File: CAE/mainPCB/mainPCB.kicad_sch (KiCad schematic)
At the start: 30 parts, among them J1 DHT22_CVT, J10 V_in_01, J12 LORA, J13 GPS_NEO, J14 VL6180X_01, J15 VL6180X_02, J2 V_In, J3 LM3144_CVT, J4 LM3144_RPM, J5 DS18B20_01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

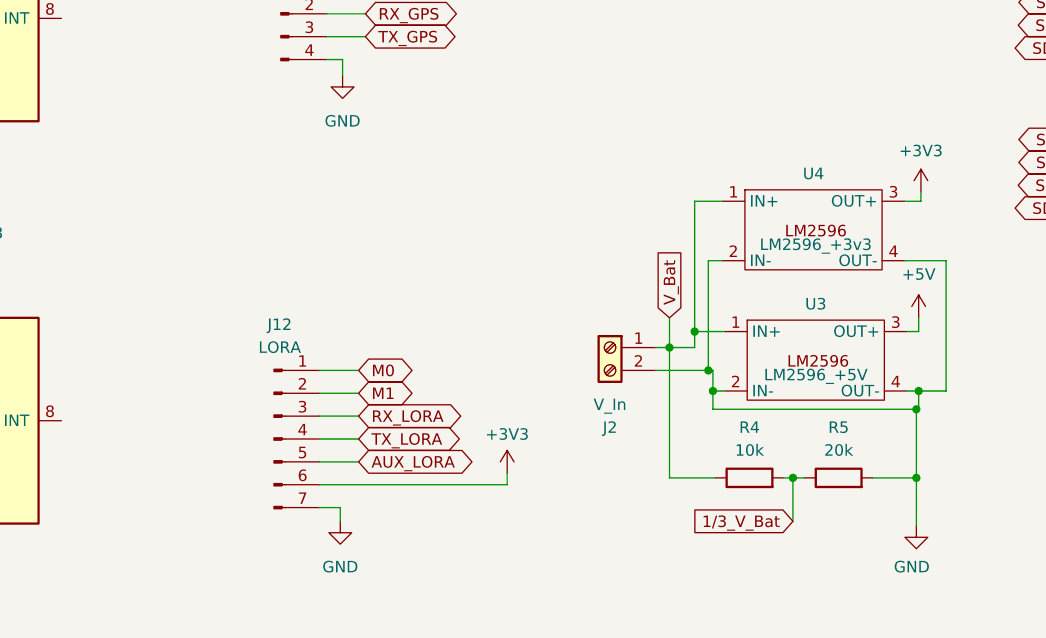
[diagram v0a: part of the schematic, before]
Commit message: PCB updated
3D models added, rewiring for milling
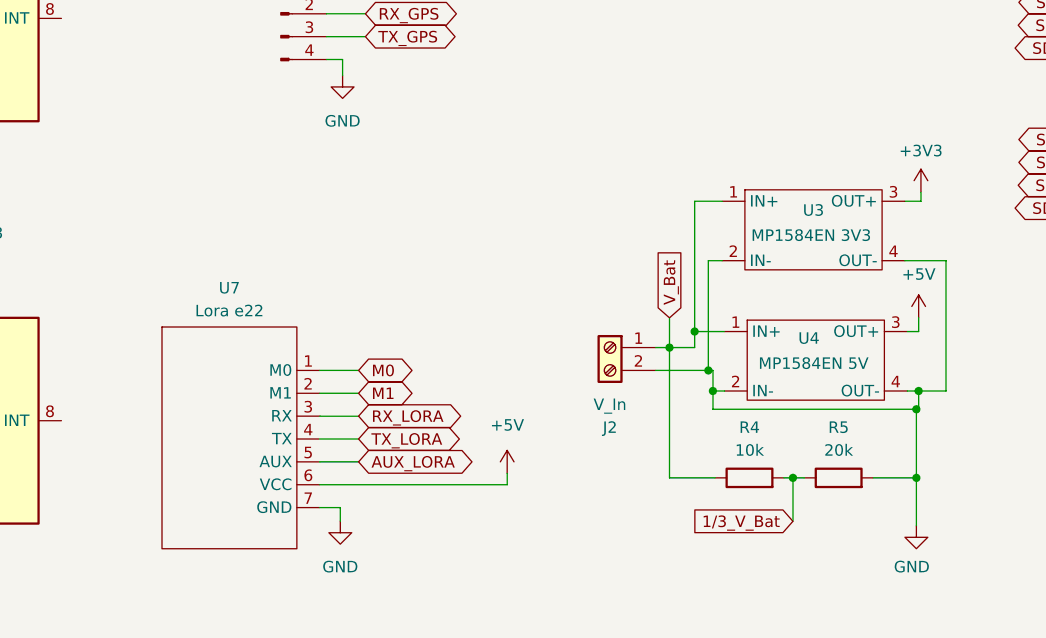
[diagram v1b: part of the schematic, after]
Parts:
- removed J12: LORA, Connector_PinHeader_2.54mm:PinHeader_1x07_P2.54mm_Vertical, symbol Connector:Conn_01x07_Pin
- removed U3: LM2596_+5V, DC_DC_LM2596_small:DC_DC_LM2596_small, symbol custom_symbols:LM2596
- removed U4: LM2596_+3v3, DC_DC_LM2596_small:DC_DC_LM2596_small, symbol custom_symbols:LM2596
- added U3: MP1584EN 3V3, custom:MP1584EN, symbol custom_symbols:MP1584EN
- added U4: MP1584EN 5V, custom:MP1584EN, symbol custom_symbols:MP1584EN
- added U7: Lora e22, custom:lora_e22, symbol custom_symbols:lora_e22
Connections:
- net +3V3: now also U3.3 (OUT+)
- net +5V: now also U4.3 (OUT+), U7.6 (VCC)
- net AUX_LORA: now also U7.5 (AUX)
- net GND: now also U3.2 (IN-), U3.4 (OUT-), U4.2 (IN-), U4.4 (OUT-), U7.7 (GND)
- net M0: now also U7.1 (M0)
- net M1: now also U7.2 (M1)
- net RX_LORA: now also U7.3 (RX)
- net TX_LORA: now also U7.4 (TX)
- net V_Bat: now also U3.1 (IN+), U4.1 (IN+)
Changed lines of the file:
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@@
-    )
-  )
-  (symbol (lib_id "custom_symbols:LM2596") (at 131.064 158.75 0) (unit 1)
-    (in_bom yes) (on_board yes) (dnp no)
-    (property "Reference" "U4" (at 131.572 152.4 0)
-      (effects (font (size 1.27 1.27)))
-    )
-    (property "Value" "LM2596_+3v3" (at 131.826 160.274 0)
-      (effects (font (size 1.27 1.27)))
-    )
-    (property "Footprint" "DC_DC_LM2596_small:DC_DC_LM2596_small" (at 131.064 158.75 0)
-      (effects (font (size 1.27 1.27)) hide)
-    )
-    (property "Datasheet" "" (at 131.064 158.75 0)
-      (effects (font (size 1.27 1.27)) hide)
-    )
-    (pin "1")
-    (pin "2")
-    (pin "3")
-    (pin "4")
-    (instances
-      (project "mainPCB"
-        (path "/e22f6e21-5f56-40d7-a167-8d60c5e75c75"
-          (reference "U4") (unit 1)
-        )
-      )
     )
   )
@@
         (path "/e22f6e21-5f56-40d7-a167-8d60c5e75c75"
           (reference "J4") (unit 1)
-        )
-      )
-    )
-  )
-  (symbol (lib_id "power:+3V3") (at 97.536 185.674 0) (unit 1)
-    (in_bom yes) (on_board yes) (dnp no) (fields_autoplaced)
-    (property "Reference" "#PWR031" (at 97.536 189.484 0)
-      (effects (font (size 1.27 1.27)) hide)
-    )
-    (property "Value" "+3V3" (at 97.536 181.356 0)
-      (effects (font (size 1.27 1.27)))
-    )
-    (property "Footprint" "" (at 97.536 185.674 0)
-      (effects (font (size 1.27 1.27)) hide)
-    )
-    (property "Datasheet" "" (at 97.536 185.674 0)
-      (effects (font (size 1.27 1.27)) hide)
-    )
-    (pin "1")
-    (instances
-      (project "mainPCB"
-        (path "/e22f6e21-5f56-40d7-a167-8d60c5e75c75"
-          (reference "#PWR031") (unit 1)
-        )
-      )
-    )
-  )
-  (symbol (lib_id "custom_symbols:LM2596") (at 131.318 173.228 0) (unit 1)
-    (in_bom yes) (on_board yes) (dnp no)
-    (property "Reference" "U3" (at 131.826 166.878 0)
-      (effects (font (size 1.27 1.27)))
-    )
-    (property "Value" "LM2596_+5V" (at 131.826 174.752 0)
-      (effects (font (size 1.27 1.27)))
-    )
-    (property "Footprint" "DC_DC_LM2596_small:DC_DC_LM2596_small" (at 131.318 173.228 0)
-      (effects (font (size 1.27 1.27)) hide)
-    )
-    (property "Datasheet" "" (at 131.318 173.228 0)
-      (effects (font (size 1.27 1.27)) hide)
-    )
-    (pin "1")
-    (pin "2")
-    (pin "3")
-    (pin "4")
-    (instances
-      (project "mainPCB"
-        (path "/e22f6e21-5f56-40d7-a167-8d60c5e75c75"
-          (reference "U3") (unit 1)
         )
       )
@@
     )
   )
-  (symbol (lib_id "Connector:Conn_01x07_Pin") (at 71.628 181.864 0) (unit 1)
-    (in_bom yes) (on_board yes) (dnp no) (fields_autoplaced)
-    (property "Reference" "J12" (at 72.263 169.164 0)
-      (effects (font (size 1.27 1.27)))
-    )
-    (property "Value" "LORA" (at 72.263 171.704 0)
-      (effects (font (size 1.27 1.27)))
-    )
-    (property "Footprint" "Connector_PinHeader_2.54mm:PinHeader_1x07_P2.54mm_Vertical" (at 71.628 181.864 0)
-      (effects (font (size 1.27 1.27)) hide)
-    )
-    (property "Datasheet" "~" (at 71.628 181.864 0)
-      (effects (font (size 1.27 1.27)) hide)
-    )
-    (pin "1")
-    (pin "2")
-    (pin "3")
-    (pin "4")
-    (pin "5")
-    (pin "6")
-    (pin "7")
-    (instances
-      (project "mainPCB"
-        (path "/e22f6e21-5f56-40d7-a167-8d60c5e75c75"
-          (reference "J12") (unit 1)
-        )
-      )
-    )
-  )
   (symbol (lib_id "power:+5V") (at 143.256 168.402 0) (unit 1)
     (in_bom yes) (on_board yes) (dnp no) (fields_autoplaced)
@@
     )
   )
+  (symbol (lib_id "custom_symbols:MP1584EN") (at 131.318 173.228 0) (unit 1)
+    (in_bom yes) (on_board yes) (dnp no)
+    (property "Reference" "U4" (at 131.064 170.688 0)
+      (effects (font (size 1.27 1.27)))
+    )
+    (property "Value" "MP1584EN 5V" (at 131.572 173.482 0)
+      (effects (font (size 1.27 1.27)))
+    )
+    (property "Footprint" "custom:MP1584EN" (at 131.318 173.228 0)
+      (effects (font (size 1.27 1.27)) hide)
+    )
+    (property "Datasheet" "" (at 131.318 173.228 0)
+      (effects (font (size 1.27 1.27)) hide)
+    )
+    (pin "1")
+    (pin "2")
+    (pin "3")
+    (pin "4")
+    (instances
+      (project "mainPCB"
+        (path "/e22f6e21-5f56-40d7-a167-8d60c5e75c75"
+          (reference "U4") (unit 1)
+        )
+      )
+    )
+  )
+  (symbol (lib_id "custom_symbols:MP1584EN") (at 131.064 158.75 0) (unit 1)
+    (in_bom yes) (on_board yes) (dnp no)
+    (property "Reference" "U3" (at 131.572 156.464 0)
+      (effects (font (size 1.27 1.27)))
+    )
+    (property "Value" "MP1584EN 3V3" (at 131.318 159.258 0)
+      (effects (font (size 1.27 1.27)))
+    )
+    (property "Footprint" "custom:MP1584EN" (at 131.064 158.75 0)
+      (effects (font (size 1.27 1.27)) hide)
+    )
+    (property "Datasheet" "" (at 131.064 158.75 0)
+      (effects (font (size 1.27 1.27)) hide)
+    )
+    (pin "1")
+    (pin "2")
+    (pin "3")
+    (pin "4")
+    (instances
+      (project "mainPCB"
+        (path "/e22f6e21-5f56-40d7-a167-8d60c5e75c75"
+          (reference "U3") (unit 1)
+        )
+      )
+    )
+  )
   (symbol (lib_id "power:+5V") (at 93.472 37.846 0) (unit 1)
     (in_bom yes) (on_board yes) (dnp no) (fields_autoplaced)
@@
         (path "/e22f6e21-5f56-40d7-a167-8d60c5e75c75"
           (reference "#PWR012") (unit 1)
+        )
+      )
+    )
+  )
+  (symbol (lib_id "custom_symbols:lora_e22") (at 67.818 181.61 0) (unit 1)
+    (in_bom yes) (on_board yes) (dnp no) (fields_autoplaced)
+    (property "Reference" "U7" (at 66.675 165.1 0)
+      (effects (font (size 1.27 1.27)))
+    )
+    (property "Value" "Lora e22" (at 66.675 167.64 0)
+      (effects (font (size 1.27 1.27)))
+    )
+    (property "Footprint" "custom:lora_e22" (at 72.136 181.61 0)
+      (effects (font (size 1.27 1.27)) hide)
+    )
+    (property "Datasheet" "" (at 72.136 181.61 0)
+      (effects (font (size 1.27 1.27)) hide)
+    )
+    (pin "1")
+    (pin "2")
+    (pin "3")
+    (pin "4")
+    (pin "5")
+    (pin "6")
+    (pin "7")
+    (instances
+      (project "mainPCB"
+        (path "/e22f6e21-5f56-40d7-a167-8d60c5e75c75"
+          (reference "U7") (unit 1)
         )
       )
@@
         )
       )
+    )
+  )
+  (symbol (lib_id "power:+5V") (at 97.536 185.674 0) (unit 1)
+    (in_bom yes) (on_board yes) (dnp no) (fields_autoplaced)
+    (property "Reference" "#PWR04" (at 97.536 189.484 0)
+      (effects (font (size 1.27 1.27)) hide)
+    )
+    (property "Value" "+5V" (at 97.536 180.34 0)
+      (effects (font (size 1.27 1.27)))
+    )
+    (property "Footprint" "" (at 97.536 185.674 0)
+      (effects (font (size 1.27 1.27)) hide)
+    )
+    (property "Datasheet" "" (at 97.536 185.674 0)
+      (effects (font (size 1.27 1.27)) hide)
+    )
+    (pin "1")
+    (instances
+      (project "mainPCB"
+        (path "/e22f6e21-5f56-40d7-a167-8d60c5e75c75"
+          (reference "#PWR04") (unit 1)
+        )
+      )

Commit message: PCB design updated
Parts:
- added A4, A5: MPU6050_Module, Charleslabs_Parts:MPU6050_Module, symbol Charleslabs_Parts:MPU6050_Module
- added J11: OpenLog TX, Connector_PinHeader_2.54mm:PinHeader_1x02_P2.54mm_Vertical, symbol Connector:Conn_01x02_Pin
- added J12: MPU6050_1, Connector_PinHeader_2.54mm:PinHeader_1x04_P2.54mm_Vertical, symbol Connector:Conn_01x04_Pin
- added Q1, Q2: BSS138, Package_TO_SOT_SMD:SOT-23, symbol Transistor_FET:BSS138
- added R10, R11, R7, R9: R10K, Resistor_THT:R_Axial_DIN0207_L6.3mm_D2.5mm_P7.62mm_Horizontal, symbol Device:R
- added U8: Neo GPS, custom:neo_gps, symbol custom_symbols:neo_gps
- J13: value GPS_NEO -> MPU6050_2
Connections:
- net +3V3: now also A4.1 (VCC), A4.7 (AD0), A5.1 (VCC), J12.1 (Pin_1), Q1.1 (G), Q2.1 (G), R10.1, R7.1, U8.4 (3V3)
- net +5V: now also R11.1, R9.1
- net GND: now also A4.2 (GND), A5.2 (GND), A5.7 (AD0), J12.4 (Pin_4), U8.1 (GND)
- net M0: now also U2.9 (25); no longer U2.21 (23)
- net M1: now also U2.21 (23); no longer U2.22
- net RX_GPS: now also U1.28 (18), U8.3 (RX); no longer J13.2 (Pin_2), U1.12 (14)
- net RX_LORA: now also U2.30 (17); no longer U2.23 (TX)
- net SDA_01_L: now also U2.25 (21), J12.3 (Pin_3)
- net SLC_01_L: now also U2.22, J12.2 (Pin_2)
- net TX_GPS: now also U1.27 (19), U8.2 (TX); no longer J13.3 (Pin_3), U1.13 (12)
- net TX_LORA: now also U2.31 (16); no longer U2.24 (RX)
- net at J5.2 (Pin_2), J7.2 (Pin_2), R2.1: now also U2.8 (33); no longer U2.6 (35)
- net SDA_02_L: now reaches U2.10 (26)
- net SDA_02_L: now also J13.3 (Pin_3), A4.4 (SDA), A5.4 (SDA)
- net SLC_02_L: now reaches U2.11 (27)
- net SLC_02_L: now also J13.2 (Pin_2), A4.3 (SCL), A5.3 (SCL)
- net RX_ESP32: no longer names the net of U2.16 (D2)
- net RX_ESP32: no longer U1.16 (D2)
- net RX_OpenLog_H: no longer names the net of U5.5 (RX0)
- net RX_OpenLog_H: now also Q1.3 (D), R9.2; no longer U6.14 (B6)
- net RX_OpenLog_L: no longer names the net of U2.29 (5)
- net RX_OpenLog_L: no longer U6.8 (A7)
- net TX_ESP32: no longer names the net of U2.17 (D3)
- net TX_ESP32: no longer U1.17 (D3)
- net TX_OpenLog_H: no longer names the net of U6.13 (B7)
- net TX_OpenLog_H: no longer U5.4 (TX0)
- net TX_OpenLog_L: no longer names the net of U2.32 (4)
- net TX_OpenLog_L: no longer U6.7 (A6)
- new net: Q1.2 (S), R7.2, U2.23 (TX)
- new net: J11.1 (Pin_1), U2.24 (RX)
- new net: J11.2 (Pin_2), Q2.2 (S), R10.2
- new net: Q2.3 (D), R11.2, U5.4 (TX0)
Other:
- company: (none) -> Escuadron UAM
- title: (none) -> Data acquisition and transmission Schematic
- moved on the sheet: A1, A2, A3, J1, J10, J14, J15, J2, J3, J4, J5, J6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
